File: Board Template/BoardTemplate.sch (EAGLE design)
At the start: 1 part

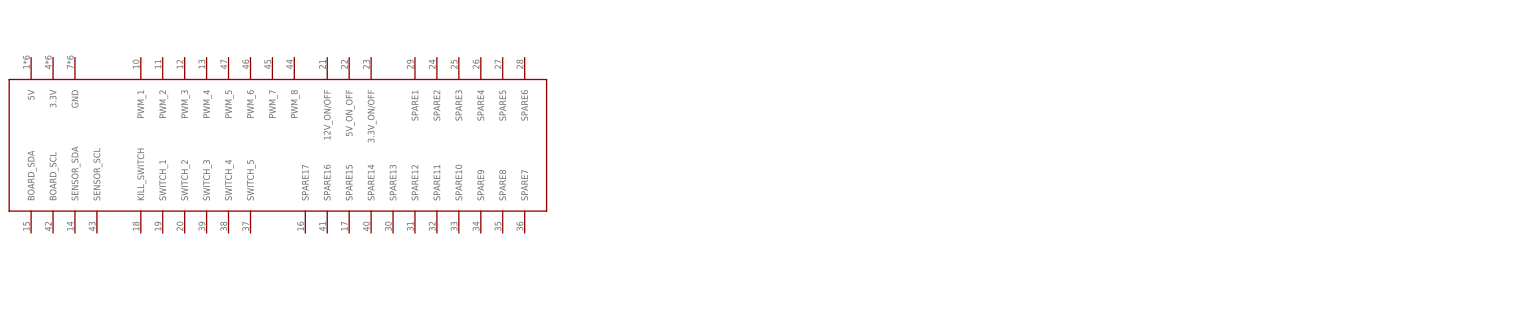
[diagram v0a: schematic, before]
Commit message: New schematic template and converter fixes
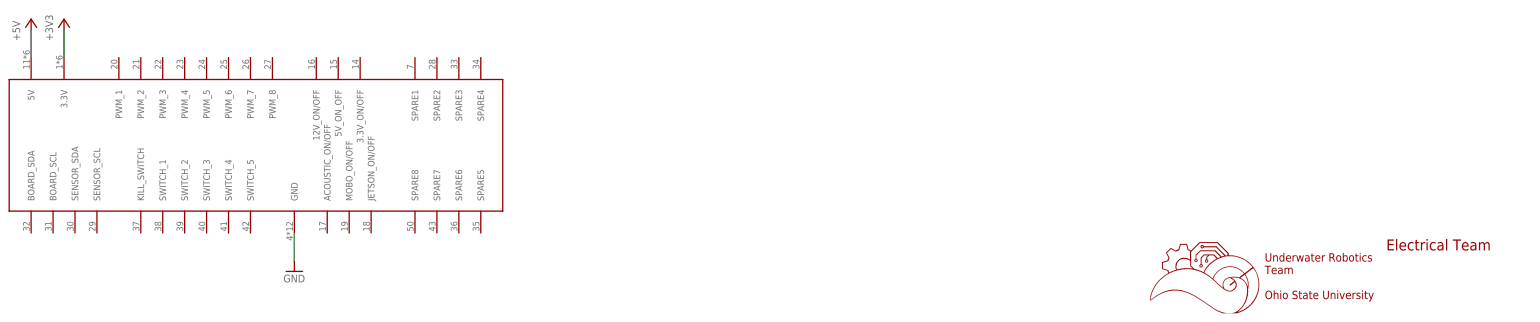
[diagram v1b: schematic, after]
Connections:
- new net +3V3: U$1.3.3V
- new net +5V: U$1.5V
- new net GND: U$1.GND
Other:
- note added: "Electrical Team"
- note added: "Underwater Robotics Team Ohio State University"
